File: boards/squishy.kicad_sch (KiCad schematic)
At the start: 56 parts, among them J1 USB_B_Micro, J2 Conn_02x26_Top_Bottom, J3 Conn_01x04, J4 Conn_02x05_Odd_Even, Q1 Q_PMOS_DGS, U12 SP3400-02UTG, U14 USB3318, U19 ICE40HX8K-BG121, U26 W25N01GVZEIG, X1 16MHz, X2 48MHz

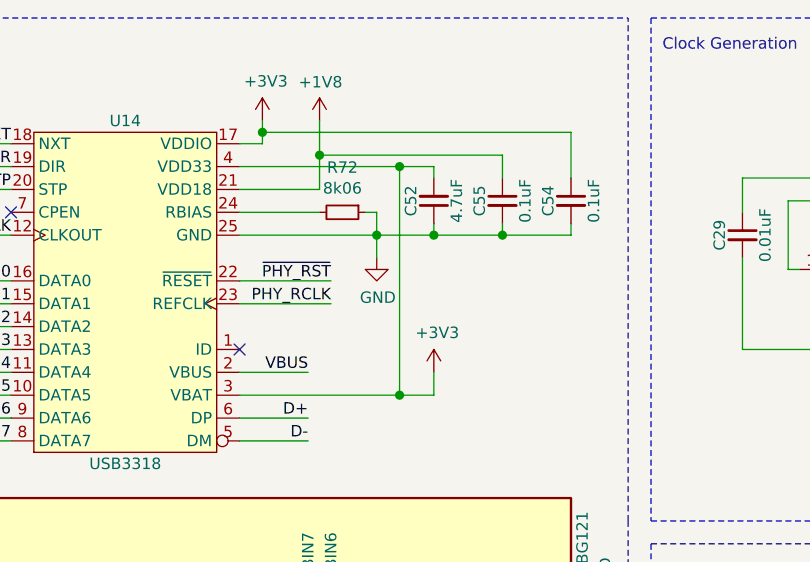
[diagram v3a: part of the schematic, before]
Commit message: hardware: added additional ground points
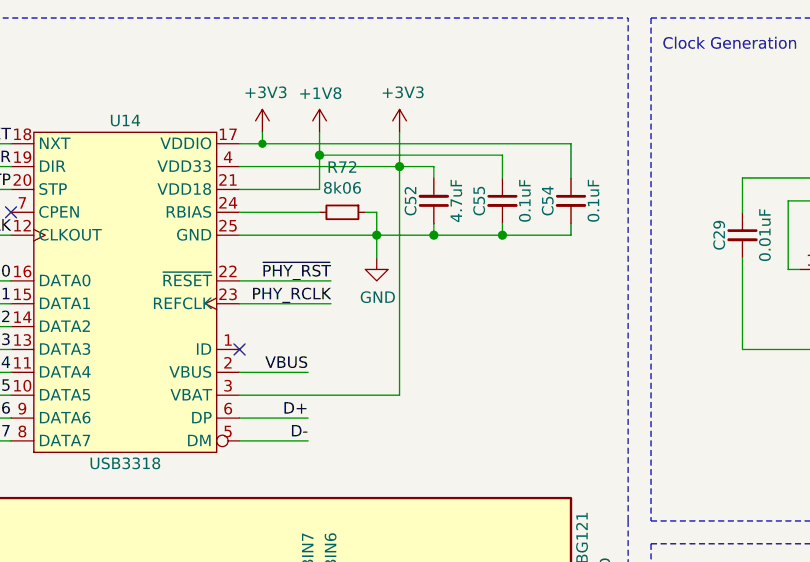
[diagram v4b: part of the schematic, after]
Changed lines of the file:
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@@
   (junction (at 109.22 233.68) (diameter 0) (color 0 0 0 0))
   (junction (at 109.22 256.54) (diameter 0) (color 0 0 0 0))
-  (junction (at 114.3 26.67) (diameter 1.016) (color 0 0 0 0))
+  (junction (at 114.3 27.94) (diameter 0) (color 0 0 0 0))
   (junction (at 120.65 29.21) (diameter 1.016) (color 0 0 0 0))
   (junction (at 127 38.1) (diameter 1.016) (color 0 0 0 0))
   (junction (at 129.54 30.48) (diameter 1.016) (color 0 0 0 0))
-  (junction (at 129.54 55.88) (diameter 1.016) (color 0 0 0 0))
   (junction (at 133.35 38.1) (diameter 1.016) (color 0 0 0 0))
   (junction (at 140.97 38.1) (diameter 1.016) (color 0 0 0 0))
@@
     (stroke (width 0) (type solid) (color 0 0 0 0))
   )
-  (wire (pts (xy 114.3 25.4) (xy 114.3 26.67))
-    (stroke (width 0) (type solid) (color 0 0 0 0))
-  )
   (wire (pts (xy 114.3 26.67) (xy 114.3 27.94))
     (stroke (width 0) (type solid) (color 0 0 0 0))
   )
-  (wire (pts (xy 114.3 26.67) (xy 148.59 26.67))
+  (wire (pts (xy 114.3 27.94) (xy 111.76 27.94))
     (stroke (width 0) (type solid) (color 0 0 0 0))
   )
-  (wire (pts (xy 114.3 27.94) (xy 111.76 27.94))
+  (wire (pts (xy 114.3 27.94) (xy 148.59 27.94))
     (stroke (width 0) (type solid) (color 0 0 0 0))
   )
@@
     (stroke (width 0) (type solid) (color 0 0 0 0))
   )
-  (wire (pts (xy 120.65 25.4) (xy 120.65 29.21))
+  (wire (pts (xy 120.65 26.67) (xy 120.65 29.21))
     (stroke (width 0) (type solid) (color 0 0 0 0))
   )
@@
     (stroke (width 0) (type solid) (color 0 0 0 0))
   )
+  (wire (pts (xy 129.54 26.67) (xy 129.54 30.48))
+    (stroke (width 0) (type default) (color 0 0 0 0))
+  )
   (wire (pts (xy 129.54 30.48) (xy 129.54 55.88))
     (stroke (width 0) (type solid) (color 0 0 0 0))
@@
     (stroke (width 0) (type solid) (color 0 0 0 0))
   )
-  (wire (pts (xy 129.54 55.88) (xy 133.35 55.88))
-    (stroke (width 0) (type solid) (color 0 0 0 0))
-  )
   (wire (pts (xy 132.08 104.14) (xy 132.08 88.9))
     (stroke (width 0) (type solid) (color 0 0 0 0))
@@
     (stroke (width 0) (type solid) (color 0 0 0 0))
   )
-  (wire (pts (xy 133.35 53.34) (xy 133.35 55.88))
-    (stroke (width 0) (type solid) (color 0 0 0 0))
-  )
   (wire (pts (xy 134.62 104.14) (xy 134.62 88.9))
     (stroke (width 0) (type solid) (color 0 0 0 0))
@@
     (stroke (width 0) (type solid) (color 0 0 0 0))
   )
-  (wire (pts (xy 148.59 26.67) (xy 148.59 31.75))
+  (wire (pts (xy 148.59 27.94) (xy 148.59 31.75))
     (stroke (width 0) (type solid) (color 0 0 0 0))
   )
@@
     (pin "1")
   )
-  (symbol (lib_id "power:+3V3") (at 114.3 25.4 0) (unit 1)
+  (symbol (lib_id "power:+3V3") (at 114.3 26.67 0) (unit 1)
     (in_bom yes) (on_board yes)
-    (property "Reference" "#PWR0113" (id 0) (at 114.3 29.21 0)
+    (property "Reference" "#PWR0113" (id 0) (at 114.3 30.48 0)
       (effects (font (size 1.27 1.27)) hide)
     )
-    (property "Value" "+3V3" (id 1) (at 114.681 21.0058 0))
-    (property "Footprint" "" (id 2) (at 114.3 25.4 0)
+    (property "Value" "+3V3" (id 1) (at 114.681 22.2758 0))
+    (property "Footprint" "" (id 2) (at 114.3 26.67 0)
       (effects (font (size 1.27 1.27)) hide)
     )
-    (property "Datasheet" "" (id 3) (at 114.3 25.4 0)
+    (property "Datasheet" "" (id 3) (at 114.3 26.67 0)
       (effects (font (size 1.27 1.27)) hide)
     )
     (pin "1")
   )
-  (symbol (lib_id "power:+1V8") (at 120.65 25.4 0) (unit 1)
+  (symbol (lib_id "power:+1V8") (at 120.65 26.67 0) (unit 1)
     (in_bom yes) (on_board yes)
-    (property "Reference" "#PWR0114" (id 0) (at 120.65 29.21 0)
+    (property "Reference" "#PWR0114" (id 0) (at 120.65 30.48 0)
       (effects (font (size 1.27 1.27)) hide)
     )
-    (property "Value" "+1V8" (id 1) (at 123.19 21.844 0)
+    (property "Value" "+1V8" (id 1) (at 123.19 23.114 0)
       (effects (font (size 1.27 1.27)) (justify right bottom))
     )
-    (property "Footprint" "" (id 2) (at 120.65 25.4 0)
+    (property "Footprint" "" (id 2) (at 120.65 26.67 0)
       (effects (font (size 1.27 1.27)) hide)
     )
-    (property "Datasheet" "" (id 3) (at 120.65 25.4 0)
+    (property "Datasheet" "" (id 3) (at 120.65 26.67 0)
       (effects (font (size 1.27 1.27)) hide)
     )
     (pin "1")
   )
-  (symbol (lib_id "power:+3V3") (at 133.35 53.34 0) (unit 1)
+  (symbol (lib_id "power:+3V3") (at 129.54 26.67 0) (unit 1)
     (in_bom yes) (on_board yes)
-    (property "Reference" "#PWR0106" (id 0) (at 133.35 57.15 0)
+    (property "Reference" "#PWR0106" (id 0) (at 129.54 30.48 0)
       (effects (font (size 1.27 1.27)) hide)
     )
-    (property "Value" "+3V3" (id 1) (at 133.731 48.9458 0))
-    (property "Footprint" "" (id 2) (at 133.35 53.34 0)
+    (property "Value" "+3V3" (id 1) (at 129.921 22.2758 0))
+    (property "Footprint" "" (id 2) (at 129.54 26.67 0)
       (effects (font (size 1.27 1.27)) hide)
     )
-    (property "Datasheet" "" (id 3) (at 133.35 53.34 0)
+    (property "Datasheet" "" (id 3) (at 129.54 26.67 0)
       (effects (font (size 1.27 1.27)) hide)
     )
@@
       (effects (font (size 1.27 1.27)) (justify left) hide)
     )
-    (property "Datasheet" "~" (id 3) (at 41.91 259.08 0)
+    (property "Datasheet" "https://www.belfuse.com/resources/datasheets/circuitprotection/ds-cp-0zch-series.pdf" (id 3) (at 41.91 259.08 0)
       (effects (font (size 1.27 1.27)) hide)
     )
@@
       (reference "#PWR0105") (unit 1) (value "GND") (footprint "")
     )
-    (path "/03bf659b-5721-4ee3-959d-52fc3ca7b16c"
+    (path "/7b9409f2-c71a-4b92-a2fe-2fd020edb85a"
       (reference "#PWR0106") (unit 1) (value "+3V3") (footprint "")
     )
@@
       (reference "#PWR0239") (unit 1) (value "GND") (footprint "")
     )
-    (path "/135fa4cc-bf68-4ed2-9d1e-cefa9ceb3983/0db0c5e8-df43-4fef-bc8b-66dcbf841b86"
-      (reference "#PWR?") (unit 1) (value "GND") (footprint "")
-    )
     (path "/135fa4cc-bf68-4ed2-9d1e-cefa9ceb3983/6f9a69da-1a3a-477d-a884-3c2a5f094604"
-      (reference "#PWR?") (unit 1) (value "GND") (footprint "")
+      (reference "#PWR0240") (unit 1) (value "GND") (footprint "")
     )
     (path "/135fa4cc-bf68-4ed2-9d1e-cefa9ceb3983/ae107d56-6c6a-46e0-b4ee-ae76a6262fca"
-      (reference "#PWR?") (unit 1) (value "+5V") (footprint "")
+      (reference "#PWR0241") (unit 1) (value "+5V") (footprint "")
+    )
+    (path "/135fa4cc-bf68-4ed2-9d1e-cefa9ceb3983/0db0c5e8-df43-4fef-bc8b-66dcbf841b86"
+      (reference "#PWR0242") (unit 1) (value "GND") (footprint "")
     )
     (path "/00000000-0000-0000-0000-00005f193b45"
@@
     )
     (path "/135fa4cc-bf68-4ed2-9d1e-cefa9ceb3983/12018f46-3cd4-4ada-98dd-ad785911f894"
-      (reference "C?") (unit 1) (value "1uF") (footprint "Capacitor_SMD:C_0603_1608Metric")
+      (reference "C70") (unit 1) (value "1uF") (footprint "Capacitor_SMD:C_0603_1608Metric")
     )
     (path "/00000000-0000-0000-0000-000072e27a6b"
@@
     )
     (path "/135fa4cc-bf68-4ed2-9d1e-cefa9ceb3983/14988e9d-0731-4f35-891c-0cdcce294cdc"
-      (reference "SW?") (unit 1) (value "RST") (footprint "lethalbit:SW_Tactile_SPST_Angled_TC-1109DE")
+      (reference "SW1") (unit 1) (value "RST") (footprint "lethalbit:SW_Tactile_SPST_Angled_TC-1109DE")
     )
     (path "/135fa4cc-bf68-4ed2-9d1e-cefa9ceb3983/e31261ca-bfe8-49da-82ba-d2d83d0636c3"
@@
       (reference "TP14") (unit 1) (value "~{TPWRE}") (footprint "TestPoint:TestPoint_Pad_D1.0mm")
     )
+    (path "/135fa4cc-bf68-4ed2-9d1e-cefa9ceb3983/e13af31a-8841-4480-be7c-2f36a354e73d"
+      (reference "TP15") (unit 1) (value "GND") (footprint "TestPoint:TestPoint_Pad_D1.0mm")
+    )
+    (path "/135fa4cc-bf68-4ed2-9d1e-cefa9ceb3983/e6f8eb40-c55c-4101-9f0d-2715bef78465"
+      (reference "TP16") (unit 1) (value "GND") (footprint "TestPoint:TestPoint_Pad_D1.0mm")
+    )
+    (path "/135fa4cc-bf68-4ed2-9d1e-cefa9ceb3983/d5e086d0-7755-45a0-8278-e7ce771b090b"
+      (reference "TP17") (unit 1) (value "GND") (footprint "TestPoint:TestPoint_Pad_D1.0mm")
+    )
+    (path "/135fa4cc-bf68-4ed2-9d1e-cefa9ceb3983/27c0c861-6f7d-4a97-8cea-a5ae9003f1a7"
+      (reference "TP18") (unit 1) (value "GND") (footprint "TestPoint:TestPoint_Pad_D1.0mm")
+    )
     (path "/5a470513-af88-45a5-8151-68e0d8ddb252/e92069a5-6c92-4eed-8047-3aa5e4866d5d"
       (reference "U1") (unit 1) (value "THVD1452DGSR") (footprint "Package_SO:VSSOP-10_3x3mm_P0.5mm")
@@
     )
     (path "/135fa4cc-bf68-4ed2-9d1e-cefa9ceb3983/3cd17d59-9727-4c74-8a44-5692d0e356fa"
-      (reference "U?") (unit 1) (value "APX811-40UG-7") (footprint "Package_TO_SOT_SMD:SOT-143")
+      (reference "U35") (unit 1) (value "APX811-40UG-7") (footprint "Package_TO_SOT_SMD:SOT-143")
     )
     (path "/b815a8ec-c187-4e06-9203-b853a6ecfa93"

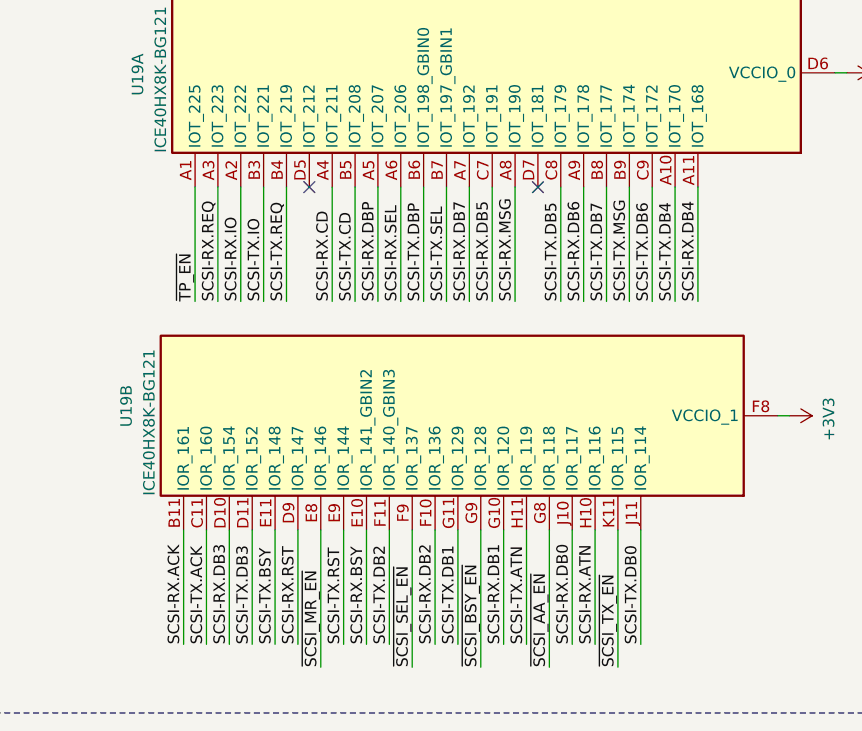
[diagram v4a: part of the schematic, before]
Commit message: hardware: supposedly fixed the pin ordering for all the scsi stuff, i hope
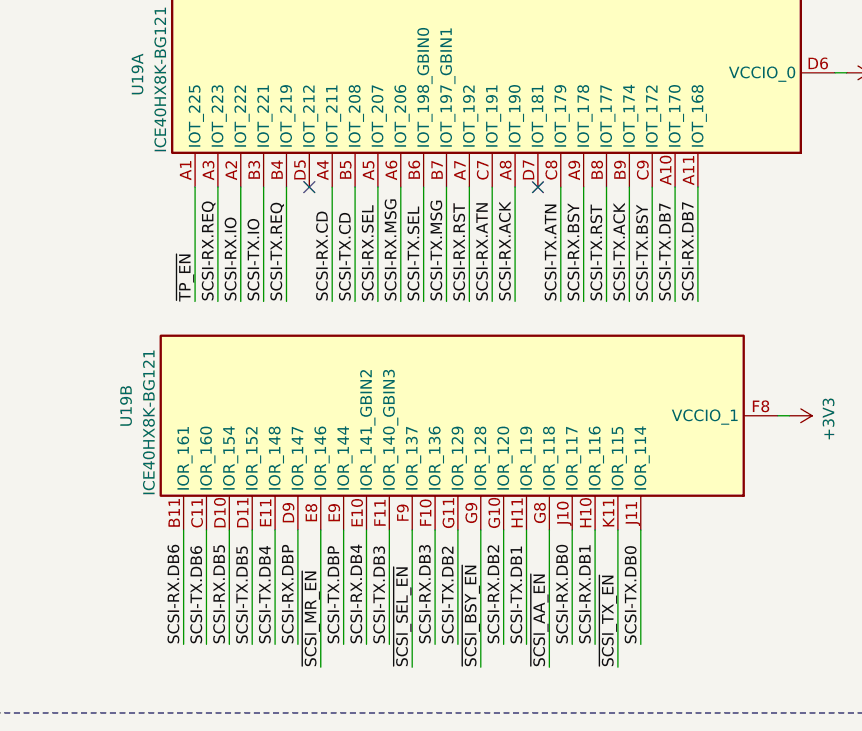
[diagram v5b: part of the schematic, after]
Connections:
- net SCSI-RX.ACK: now also U19.A8 (IOT_190); no longer U19.B11 (IOR_161)
- net SCSI-RX.ATN: now also U19.C7 (IOT_191); no longer U19.H10 (IOR_116)
- net SCSI-RX.BSY: now also U19.A9 (IOT_178); no longer U19.E10 (IOR_141_GBIN2)
- net SCSI-RX.DB1: now also U19.H10 (IOR_116); no longer U19.G10 (IOR_120)
- net SCSI-RX.DB2: now also U19.G10 (IOR_120); no longer U19.F10 (IOR_136)
- net SCSI-RX.DB3: now also U19.F10 (IOR_136); no longer U19.D10 (IOR_154)
- net SCSI-RX.DB4: now also U19.E10 (IOR_141_GBIN2); no longer U19.A11 (IOT_168)
- net SCSI-RX.DB5: now also U19.D10 (IOR_154); no longer U19.C7 (IOT_191)
- net SCSI-RX.DB6: now also U19.B11 (IOR_161); no longer U19.A9 (IOT_178)
- net SCSI-RX.DB7: now also U19.A11 (IOT_168); no longer U19.A7 (IOT_192)
- net SCSI-RX.DBP: now also U19.D9 (IOR_147); no longer U19.A5 (IOT_207)
- net SCSI-RX.MSG: now also U19.A6 (IOT_206); no longer U19.A8 (IOT_190)
- net SCSI-RX.RST: now also U19.A7 (IOT_192); no longer U19.D9 (IOR_147)
- net SCSI-RX.SEL: now also U19.A5 (IOT_207); no longer U19.A6 (IOT_206)
- net SCSI-TX.ACK: now also U19.B9 (IOT_174); no longer U19.C11 (IOR_160)
- net SCSI-TX.ATN: now also U19.C8 (IOT_179); no longer U19.H11 (IOR_119)
- net SCSI-TX.BSY: now also U19.C9 (IOT_172); no longer U19.E11 (IOR_148)
- net SCSI-TX.DB1: now also U19.H11 (IOR_119); no longer U19.G11 (IOR_129)
- net SCSI-TX.DB2: now also U19.G11 (IOR_129); no longer U19.F11 (IOR_140_GBIN3)
- net SCSI-TX.DB3: now also U19.F11 (IOR_140_GBIN3); no longer U19.D11 (IOR_152)
- net SCSI-TX.DB4: now also U19.E11 (IOR_148); no longer U19.A10 (IOT_170)
- net SCSI-TX.DB5: now also U19.D11 (IOR_152); no longer U19.C8 (IOT_179)
- net SCSI-TX.DB6: now also U19.C11 (IOR_160); no longer U19.C9 (IOT_172)
- net SCSI-TX.DB7: now also U19.A10 (IOT_170); no longer U19.B8 (IOT_177)
- net SCSI-TX.DBP: now also U19.E9 (IOR_144); no longer U19.B6 (IOT_198_GBIN0)
- net SCSI-TX.MSG: now also U19.B7 (IOT_197_GBIN1); no longer U19.B9 (IOT_174)
- net SCSI-TX.RST: now also U19.B8 (IOT_177); no longer U19.E9 (IOR_144)
- net SCSI-TX.SEL: now also U19.B6 (IOT_198_GBIN0); no longer U19.B7 (IOT_197_GBIN1)
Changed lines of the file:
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@@
     (effects (font (size 1.27 1.27)) (justify right bottom))
   )
-  (label "SCSI-RX.ACK" (at 138.43 275.59 90)
+  (label "SCSI-RX.DB6" (at 138.43 275.59 90)
     (effects (font (size 1.27 1.27)) (justify left bottom))
   )
@@
     (effects (font (size 1.27 1.27)) (justify left bottom))
   )
-  (label "SCSI-TX.ACK" (at 140.97 275.59 90)
+  (label "SCSI-TX.DB6" (at 140.97 275.59 90)
     (effects (font (size 1.27 1.27)) (justify left bottom))
   )
@@
     (effects (font (size 1.27 1.27)) (justify right bottom))
   )
-  (label "SCSI-RX.DB3" (at 143.51 275.59 90)
+  (label "SCSI-RX.DB5" (at 143.51 275.59 90)
     (effects (font (size 1.27 1.27)) (justify left bottom))
   )
@@
     (effects (font (size 1.27 1.27)) (justify left bottom))
   )
-  (label "SCSI-TX.DB3" (at 146.05 275.59 90)
+  (label "SCSI-TX.DB5" (at 146.05 275.59 90)
     (effects (font (size 1.27 1.27)) (justify left bottom))
   )
@@
     (effects (font (size 1.27 1.27)) (justify left bottom))
   )
-  (label "SCSI-TX.BSY" (at 148.59 275.59 90)
+  (label "SCSI-TX.DB4" (at 148.59 275.59 90)
     (effects (font (size 1.27 1.27)) (justify left bottom))
   )
@@
     (effects (font (size 1.27 1.27)) (justify left bottom))
   )
-  (label "SCSI-RX.RST" (at 151.13 275.59 90)
+  (label "SCSI-RX.DBP" (at 151.13 275.59 90)
     (effects (font (size 1.27 1.27)) (justify left bottom))
   )
@@
     (effects (font (size 1.27 1.27)) (justify left bottom))
   )
-  (label "SCSI-TX.RST" (at 156.21 275.59 90)
+  (label "SCSI-TX.DBP" (at 156.21 275.59 90)
     (effects (font (size 1.27 1.27)) (justify left bottom))
   )
@@
     (effects (font (size 1.27 1.27)) (justify left bottom))
   )
-  (label "SCSI-RX.BSY" (at 158.75 275.59 90)
+  (label "SCSI-RX.DB4" (at 158.75 275.59 90)
     (effects (font (size 1.27 1.27)) (justify left bottom))
   )
-  (label "SCSI-RX.DBP" (at 160.02 237.49 90)
+  (label "SCSI-RX.SEL" (at 160.02 237.49 90)
     (effects (font (size 1.27 1.27)) (justify left bottom))
   )
-  (label "SCSI-TX.DB2" (at 161.29 275.59 90)
+  (label "SCSI-TX.DB3" (at 161.29 275.59 90)
     (effects (font (size 1.27 1.27)) (justify left bottom))
   )
-  (label "SCSI-RX.SEL" (at 162.56 237.49 90)
+  (label "SCSI-RX.MSG" (at 162.56 237.49 90)
     (effects (font (size 1.27 1.27)) (justify left bottom))
   )
@@
     (effects (font (size 1.27 1.27)) (justify left bottom))
   )
-  (label "SCSI-TX.DBP" (at 165.1 237.49 90)
+  (label "SCSI-TX.SEL" (at 165.1 237.49 90)
     (effects (font (size 1.27 1.27)) (justify left bottom))
   )
-  (label "SCSI-RX.DB2" (at 166.37 275.59 90)
+  (label "SCSI-RX.DB3" (at 166.37 275.59 90)
     (effects (font (size 1.27 1.27)) (justify left bottom))
   )
@@
     (effects (font (size 1.27 1.27)) (justify left bottom))
   )
-  (label "SCSI-TX.SEL" (at 167.64 237.49 90)
+  (label "SCSI-TX.MSG" (at 167.64 237.49 90)
     (effects (font (size 1.27 1.27)) (justify left bottom))
   )
-  (label "SCSI-TX.DB1" (at 168.91 275.59 90)
+  (label "SCSI-TX.DB2" (at 168.91 275.59 90)
     (effects (font (size 1.27 1.27)) (justify left bottom))
   )
-  (label "SCSI-RX.DB7" (at 170.18 237.49 90)
+  (label "SCSI-RX.RST" (at 170.18 237.49 90)
     (effects (font (size 1.27 1.27)) (justify left bottom))
   )
@@
     (effects (font (size 1.27 1.27)) (justify left bottom))
   )
-  (label "SCSI-RX.DB5" (at 172.72 237.49 90)
+  (label "SCSI-RX.ATN" (at 172.72 237.49 90)
     (effects (font (size 1.27 1.27)) (justify left bottom))
   )
-  (label "SCSI-RX.DB1" (at 173.99 275.59 90)
+  (label "SCSI-RX.DB2" (at 173.99 275.59 90)
     (effects (font (size 1.27 1.27)) (justify left bottom))
   )
-  (label "SCSI-RX.MSG" (at 175.26 237.49 90)
+  (label "SCSI-RX.ACK" (at 175.26 237.49 90)
     (effects (font (size 1.27 1.27)) (justify left bottom))
   )
-  (label "SCSI-TX.ATN" (at 176.53 275.59 90)
+  (label "SCSI-TX.DB1" (at 176.53 275.59 90)
     (effects (font (size 1.27 1.27)) (justify left bottom))
   )
@@
     (effects (font (size 1.27 1.27)) (justify left bottom))
   )
-  (label "SCSI-TX.DB5" (at 180.34 237.49 90)
+  (label "SCSI-TX.ATN" (at 180.34 237.49 90)
     (effects (font (size 1.27 1.27)) (justify left bottom))
   )
@@
     (effects (font (size 1.27 1.27)) (justify left bottom))
   )
-  (label "SCSI-RX.DB6" (at 182.88 237.49 90)
+  (label "SCSI-RX.BSY" (at 182.88 237.49 90)
     (effects (font (size 1.27 1.27)) (justify left bottom))
   )
-  (label "SCSI-RX.ATN" (at 184.15 275.59 90)
+  (label "SCSI-RX.DB1" (at 184.15 275.59 90)
     (effects (font (size 1.27 1.27)) (justify left bottom))
   )
-  (label "SCSI-TX.DB7" (at 185.42 237.49 90)
+  (label "SCSI-TX.RST" (at 185.42 237.49 90)
     (effects (font (size 1.27 1.27)) (justify left bottom))
   )
@@
     (effects (font (size 1.27 1.27)) (justify left bottom))
   )
-  (label "SCSI-TX.MSG" (at 187.96 237.49 90)
+  (label "SCSI-TX.ACK" (at 187.96 237.49 90)
     (effects (font (size 1.27 1.27)) (justify left bottom))
   )
@@
     (effects (font (size 1.27 1.27)) (justify left bottom))
   )
-  (label "SCSI-TX.DB6" (at 190.5 237.49 90)
+  (label "SCSI-TX.BSY" (at 190.5 237.49 90)
     (effects (font (size 1.27 1.27)) (justify left bottom))
   )
-  (label "SCSI-TX.DB4" (at 193.04 237.49 90)
+  (label "SCSI-TX.DB7" (at 193.04 237.49 90)
     (effects (font (size 1.27 1.27)) (justify left bottom))
   )
@@
     (effects (font (size 1.27 1.27)) (justify left bottom))
   )
-  (label "SCSI-RX.DB4" (at 195.58 237.49 90)
+  (label "SCSI-RX.DB7" (at 195.58 237.49 90)
     (effects (font (size 1.27 1.27)) (justify left bottom))
   )
